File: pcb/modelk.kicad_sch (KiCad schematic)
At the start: 38 parts, among them J1 Battery Conn, J2 Conn_01x20, J3 Conn_01x05, J4 Conn_01x12, J5 Conn_01x04, J6 Conn_01x08, SW1 SW_reset, U1 nice_nano, U2 74HC595, U3 74HC595, U4 74HC595

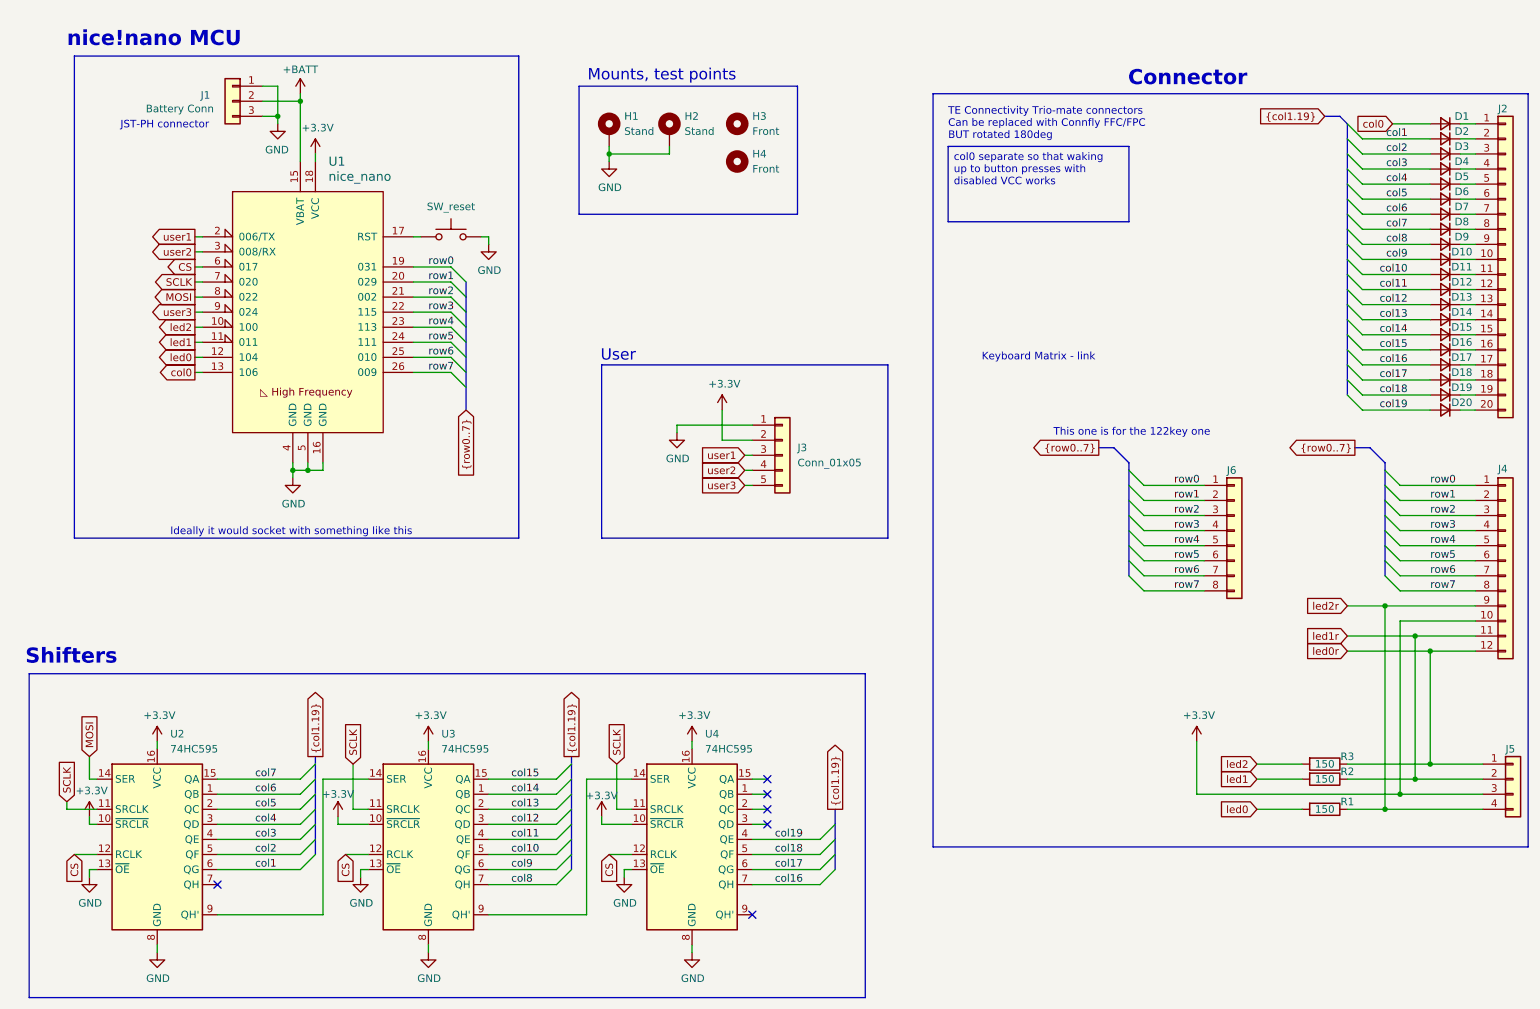
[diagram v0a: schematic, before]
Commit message: Added faston ground connector
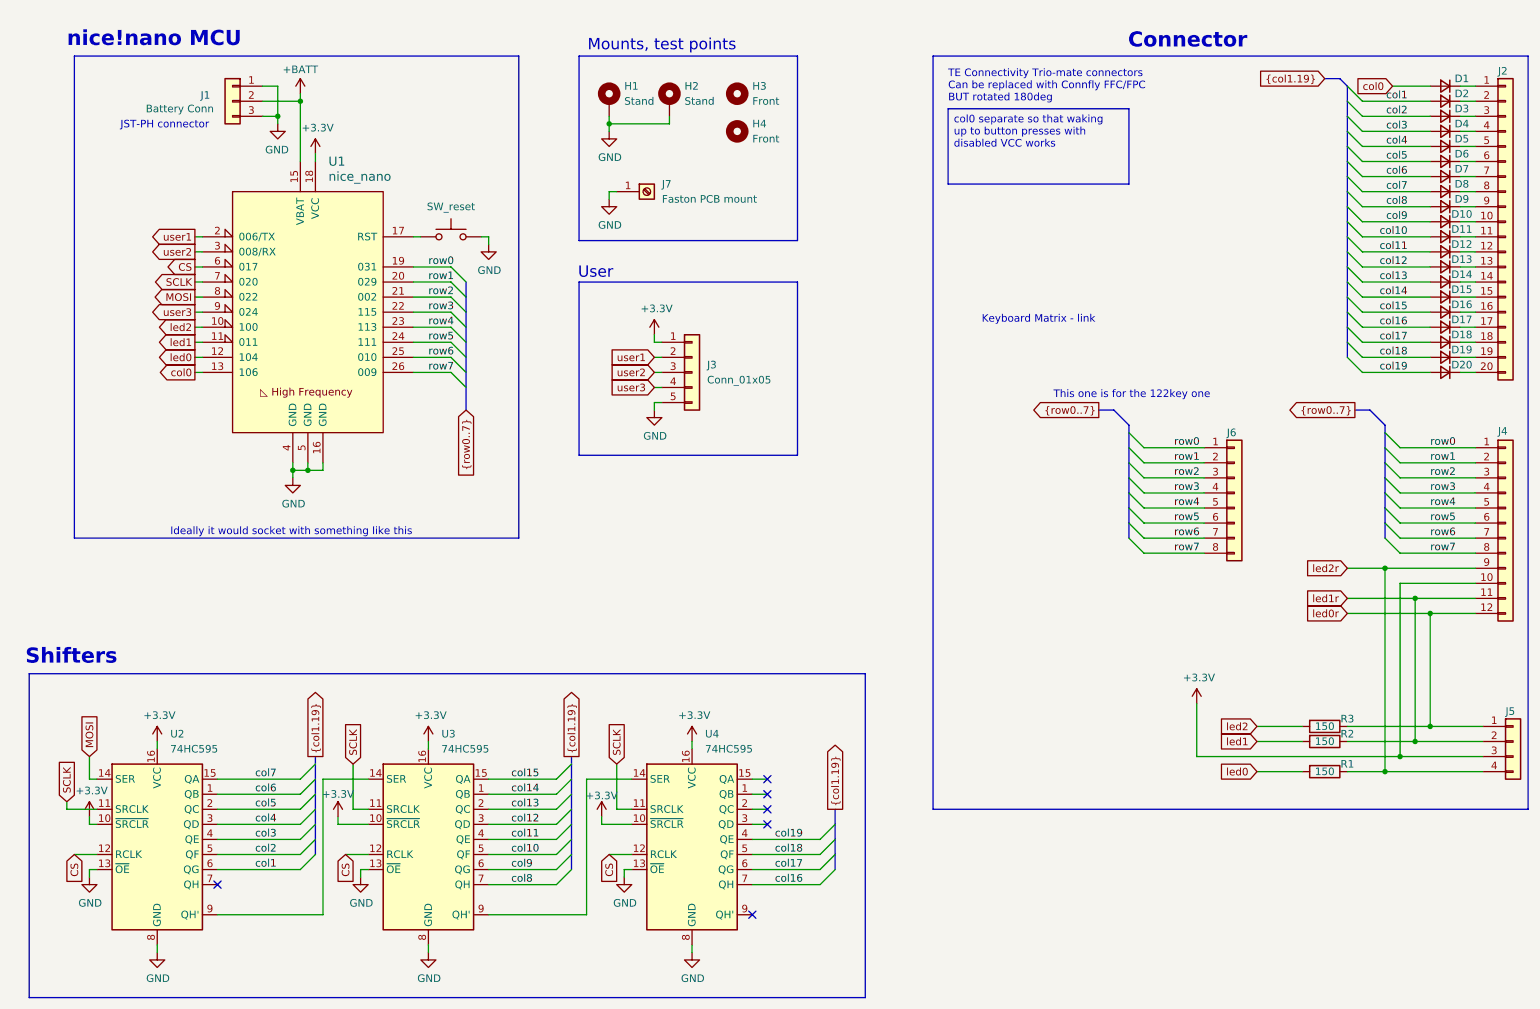
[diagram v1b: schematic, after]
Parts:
- added J7: Faston PCB mount, Library:faston-mount, symbol Connector:Screw_Terminal_01x01
- J3: now left out of the parts list
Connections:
- net +3.3V: now also J3.1 (Pin_1); no longer J3.2 (Pin_2)
- net GND: now also J3.5 (Pin_5), J7.1 (Pin_1); no longer J3.1 (Pin_1)
- net user1: now also J3.2 (Pin_2); no longer J3.3 (Pin_3)
- net user2: now also J3.3 (Pin_3); no longer J3.4 (Pin_4)
- net user3: now also J3.4 (Pin_4); no longer J3.5 (Pin_5)
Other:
- moved on the sheet: D1, D10, D11, D12, D13, D14, D15, D16, D17, D18, D19, D2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

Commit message: Fixed DRC
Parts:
- J1: value Battery Conn -> JST-PH connector
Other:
- note removed: "JST-PH connector"
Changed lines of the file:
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@@
 		)
 	)
-	(text "JST-PH connector"
-		(exclude_from_sim no)
-		(at 48.26 38.354 0)
-		(effects
-			(font
-				(size 1.27 1.27)
-			)
-		)
-	)
 	(text "TE Connectivity Trio-mate connectors\nCan be replaced with Connfly FFC/FPC\nBUT rotated 180deg"
 		(exclude_from_sim no)
@@
 			"AAAAAAAAAAAAAAAAAAAAAAAAAAAAAAAAAAAAAAAAAAAAAAAAAAAAAAAAAAAAAAAAAAAAAAAAAAAA"
 			"AAAAAAAAAAAAAAAAAAAAAAAAAAAAAAAAAAAAAAAAAAAAAAAAAAAAAAAAAAAAAAAAAAAAAAAAAAAA"
-			"AAAAAA=="
+			"AAAAAAAAawAAAEEAAABpAAAAYgAAAEkAAAA4AAAAMwAAAHcAAABnAAAARQAAAEkAAABBAAAAYwAA"
+			"AEEAAABCAAAAcgAAAEYAAABuAAAAcwAAAFEAAABNAAAAVQAAAEsAAABWAAAALwAAAFIAAABQAAAA"
+			"MgAAAG4AAAB3AAAAaAAAADkAAAArAAAANgAAAEgAAABRAAAANgAAADQAAABWAAAAcAAAAGwAAAB4"
+			"AAAATQAAAEMAAABHAAAAYwAAAEQAAABpAAAATQAAADUAAABhAAAAQQAAAGQAAAB3AAAAMwAAAEYA"
+			"AABGAAAASQAAADEAAAB1AAAAdwAAAEkAAABzAAAATgAAAHQAAABHAAAASwAAAGwAAAArAAAAagAA"
+			"AHoAAABNAAAARwAAAGkAAAA0AAAAaQAAADkAAABCAAAAMwAAADcAAABCAAAAaQAAAEQAAAA1AAAA"
+			"bAAAAEQAAABKAAAAbQAAAGEAAAB4AAAAcQAAAEUAAABXAAAASQAAAGkAAABSAAAASgAAAHEAAAA5"
+			"AAAAWAAAAEMAAAAwAAAAaQAAAEMAAAAxAAAAZgAAAG0AAABFAAAAKwAAAFIAAAB6AAAAUgAAAGUA"
+			"AABPAAAASQAAAHMAAABOAAAAQgAAAGcAAABNAAAARQAAAFMAAABuAAAAUQAAAFAAAABDAAAAaAAA"
+			"AFgAAABEAAAATQAAAFAAAABCAAAAVwAAAFEAAABaAAAAeQAAAGkAAABWAAAAaQAAAEsAAAA0AAAA"
+			"WgAAAGMAAABIAAAAagAAAHcAAABJAAAAbQAAAFMAAAB5AAAASwAAAHoAAABZAAAATAAAADMAAABn"
+			"AAAAWQAAAHIAAABnAAAAUAAAAHMAAABMAAAAQwAAAEoAAAB1AAAATQAAAFMAAAB3AAAAeAAAAG0A"
+			"AABMAAAAagAAAEoAAABaAAAASAAAAEsAAAA3AAAAMwAAAGEAAABBAAAATgAAAGEAAABsAAAARwAA"
+			"AEcAAABUAAAASgAAAEIAAABrAAAAQwAAAEkAAABJAAAAZwAAAFkAAABHAAAAbAAAAGcAAABzAAAA"
+			"WQAAAEEAAAA3AAAAVAAAAHEAAAB2AAAAVgAAAGcAAABnAAAAQQAAAFMAAABMAAAATwAAAFUAAABn"
+			"AAAARAAAADcAAAB2AAAAZAAAAEQAAABwAAAAWQAAAEsAAAA3AAAAaAAAAHkAAABKAAAAUgAAAEMA"
+			"AABEAAAATQAAAFEAAABhAAAATwAAAGoAAAB1AAAAaAAAAG0AAAA2AAAAUAAAAGEAAABMAAAANQAA"
+			"AEYAAABBAAAAUQAAAEIAAAB4AAAAegAAAEMAAABvAAAAbgAAAFkAAABxAAAAZQAAAGsAAABIAAAA"
+			"SgAAAA=="
 		)
 	)
@@
 		(dnp no)
 		(property "Reference" "J1"
-			(at 55.118 33.274 0)
+			(at 59.69 29.464 0)
 			(effects
 				(font
@@
 			)
 		)
-		(property "Value" "Battery Conn"
-			(at 50.8 35.56 0)
+		(property "Value" "JST-PH connector"
+			(at 55.88 39.624 0)
 			(effects
 				(font

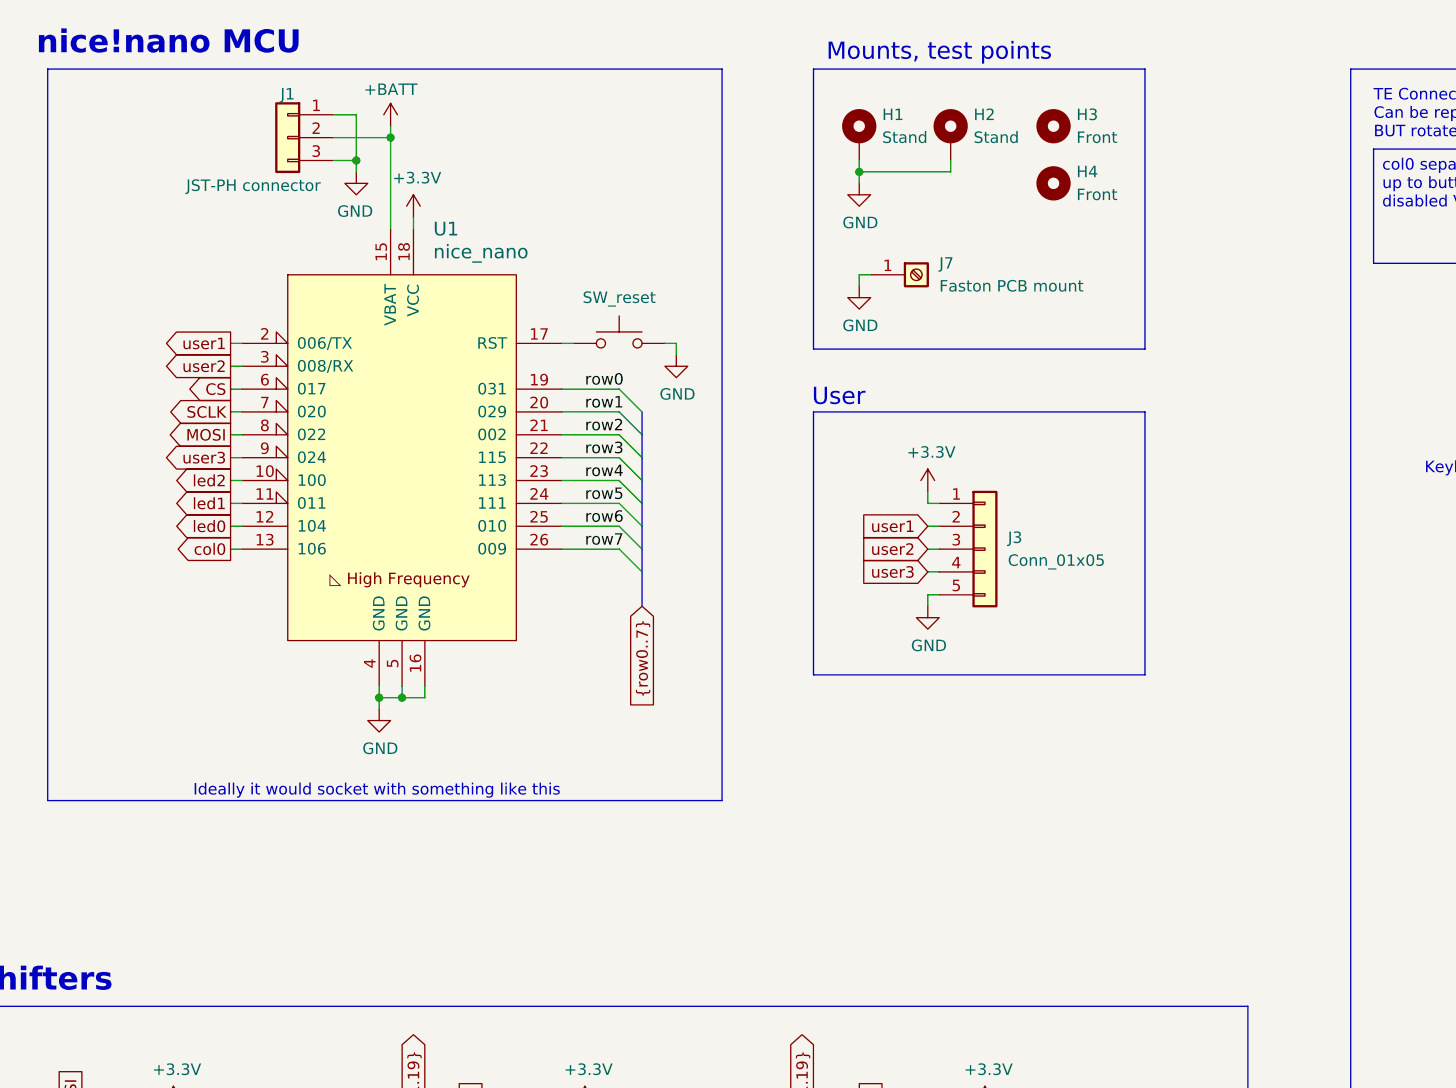
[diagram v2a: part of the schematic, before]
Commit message: Added battery header for profiling
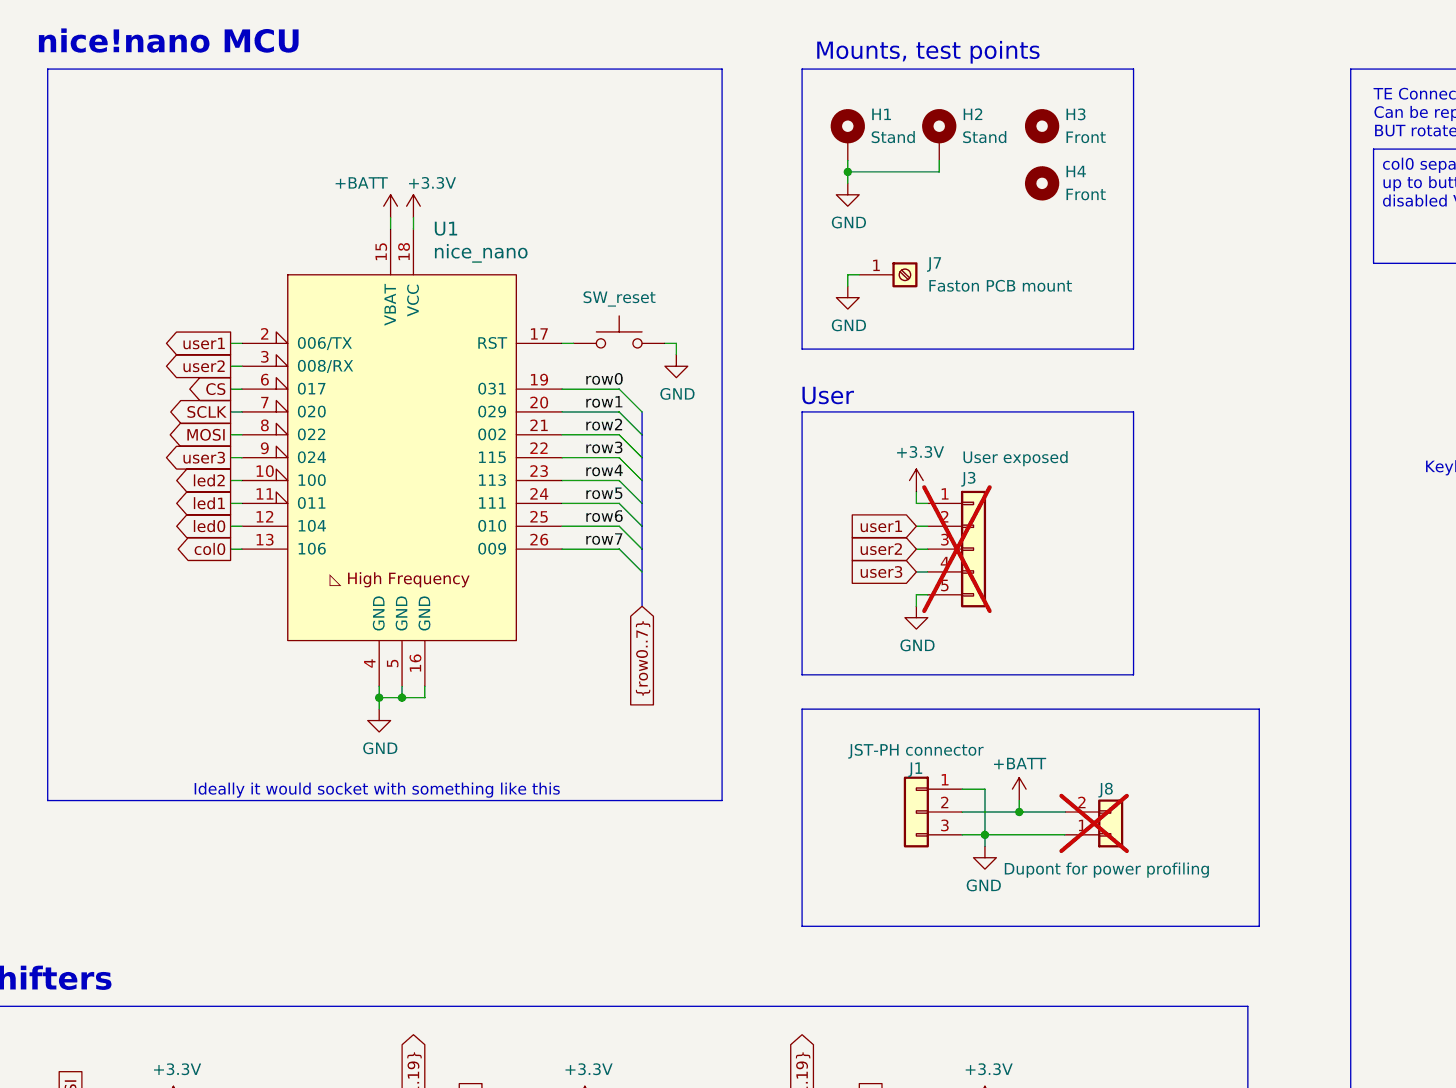
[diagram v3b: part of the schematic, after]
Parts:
- added J8: Dupont for power profiling, Library:BatteryHeader, symbol Connector_Generic:Conn_01x02
- J3: value Conn_01x05 -> User exposed; now not fitted
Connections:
- net +BATT: now also J8.2 (Pin_2)
- net GND: now also J8.1 (Pin_1)
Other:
- moved on the sheet: H1, H2, H3, H4, J1, J7

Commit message: Removed mount holes from ffc connectors
This also fixes all DRC errors.
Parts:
- J5: footprint Library:ModelH-triomate-leds4 -> Library:ffc-leds4
- J6: footprint Library:ModelH-triomate-rows8 -> Library:ffc-rows8
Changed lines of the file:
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@@
 			"AAAAAAAAAAAAAAAAAAAAAAAAAAAAAAAAAAAAAAAAAAAAAAAAAAAAAAAAAAAAAAAAAAAAAAAAAAAA"
 			"AAAAAAAAAAAAAAAAAAAAAAAAAAAAAAAAAAAAAAAAAAAAAAAAAAAAAAAAAAAAAAAAAAAAAAAAAAAA"
+			"AAAAAAAAAAAAAAAAAAAAAAAAAAAAAAAAAAAAAAAAAAAAAAAAAAAAAAAAAAAAAAAAAAAAAAAAAAAA"
+			"AAAAAAAAAAAAAAAAAAAAAAAAAAAAAAAAAAAAAAAAAAAAAAAAAAAAAAAAAAAAAAAAAAAAAAAAAAAA"
+			"AAAAAAAAAAAAAAAAAAAAAAAAAAAAAAAAAAAAAAAAAAAAAAAAAAAAAAAAAAAAAAAAAAAAAAAAAAAA"
+			"AAAAAAAAAAAAAAAAAAAAAAAAAAAAAAAAAAAAAAAAAAAAAAAAAAAAAAAAAAAAAAAAAAAAAAAAAAAA"
+			"AAAAAAAAAAAAAAAAAAAAAAAAAAAAAAAAAAAAAAAAAAAAAAAAAAAAAAAAAAAAAAAAAAAAAAAAAAAA"
+			"AAAAAAAAAAAAAAAAAAAAAAAAAAAAAAAAAAAAAAAAAAAAAAAAAAAAAAAAAAAAAAAAAAAAAAAAAAAA"
+			"AAAAAAAAAAAAAAAAAAAAAAAAAAAAAAAAAAAAAAAAAAAAAAAAAAAAAAAAAAAAAAAAAAAAAAAAAAAA"
+			"AAAAAAAAAAAAAAAAAAAAoTYAAAAAAACgVvVKAAAAADBHHUsAAAAAAAAAAAAAAAAAAAAAAAAAABBK"
+			"9vNnfwAAFdzGQyRaT+aa3ncTfaXM9jAAAAAAAAAAMFrvSgAAAAAAAAAAzAMAAAAAAAAAAAAAAAAA"
+			"AAAAAAAAAAAAAAAAAAAAAAAAAAAAAAAAAAAAAAAAAAAAAAAAACD19EoAAAAAIPX0SgAAAAAAAAAA"
+			"AAAAAHj19EoAAAAAAQAAAAAAAAAAAAAAAAAAAAAAAAAAAAAAAACAPwAAAAAAAAAAAAAAAAAAAAAA"
+			"AAAAAAAAAAAAAAC49fRKAAAAAAEAAAAAAAAAAAAAAAAAAAAAAAAAAAAAAAAAgD8AAAAAAAAAAAAA"
+			"AAAAAAAAAAAAAMhD8PNnfwAA2PX0SgAAAAAAAAAAAAAAAAAAAAAAAAAAAAAAAAAAAAAAAAAAAAAA"
+			"AAAAAAAAAAAAkHW682d/AACQDu9KAAAAAAYAAAAAAAAABgAAAAAAAAAAAAAAAAAAAFAN00sAAAAA"
+			"BgAAAAAAAAAAZNVRAAAAAAYAAAAAAAAABgAAAAAAAAAAAAAAAAAAAAAAAAAAAAAAAAAAAAAAAAAA"
+			"AAAAAAAAAHj29EoAAAAAAAAAAAAAAAAAAAAAAAAAAAAAAAAAAAAAAAAAAAAAAAAAAAAAAAAAAAAA"
+			"AAAAAAAAAAAAAAAAAAAAAAAAAAAAAAAAAAAAAAAAAAAAAAAAAAAAAAAAAAAAAAAAAAAAAAAAAAAA"
+			"AAAAAAAAAAAAAAAAAND29EoAAAAA0Pb0SgAAAAAAAAAAAAAAAAAAAAAAAAAAAAAAAAAAAAAAAAAA"
 			"AAAAAA=="
 		)
@@
 			)
 		)
-		(property "Footprint" "Library:ModelH-triomate-leds4"
+		(property "Footprint" "Library:ffc-leds4"
 			(at 275.59 142.24 0)
 			(effects
@@
 			)
 		)
-		(property "Footprint" "Library:ModelH-triomate-rows8"
+		(property "Footprint" "Library:ffc-rows8"
 			(at 228.6 100.33 0)
 			(effects

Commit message: Actions test
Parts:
- J2: footprint Library:ModelH-triomate-cols20 -> Library:ffc-cols20
- J4: footprint Library:ModelH-triomate-rows12 -> Library:ffc-rows12
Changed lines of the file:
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@@
 			)
 		)
-		(property "Footprint" "Library:ModelH-triomate-rows12"
+		(property "Footprint" "Library:ffc-rows12"
 			(at 274.32 105.41 0)
 			(effects
@@
 		(at 132.08 34.29 0)
 		(unit 1)
-		(exclude_from_sim yes)
+		(exclude_from_sim no)
 		(in_bom no)
 		(on_board yes)
@@
 		(at 121.92 34.29 0)
 		(unit 1)
-		(exclude_from_sim yes)
+		(exclude_from_sim no)
 		(in_bom no)
 		(on_board yes)
@@
 			)
 		)
-		(property "Footprint" "Library:ModelH-triomate-cols20"
+		(property "Footprint" "Library:ffc-cols20"
 			(at 274.32 54.61 0)
 			(effects
@@
 		(at 143.51 33.02 0)
 		(unit 1)
-		(exclude_from_sim yes)
+		(exclude_from_sim no)
 		(in_bom no)
 		(on_board yes)
@@
 		)
 		(property "Datasheet" "https://nicekeyboards.com/docs/nice-nano/pinout-schematic"
-			(at 99.06 132.08 90)
+			(at 72.39 30.226 0)
 			(effects
 				(font
@@
 		(at 143.51 39.37 0)
 		(unit 1)
-		(exclude_from_sim yes)
+		(exclude_from_sim no)
 		(in_bom no)
 		(on_board yes)
